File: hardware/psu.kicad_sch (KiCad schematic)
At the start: 35 parts, among them J1 12V Barrel, J2 12V Screw Terminal, Q1 FDS4435BZ, U1 NCP1117-3.3_SOT223, U2 AP64501SP-13

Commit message: Switch AP64501 to standard KiCad SOIC-8-EP footprint
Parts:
- U2: footprint granit:SOIC-8-1EP_3.9x4.9mm_P1.27mm_EP2.95x4.9mm_Mask2.71x3.4mm_ThermalVias -> Package_SO:SOIC-8-1EP_3.9x4.9mm_P1.27mm_EP2.95x4.9mm_Mask2.71x3.4mm_ThermalVias
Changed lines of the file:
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@@
 			)
 		)
-		(property "Footprint" "granit:SOIC-8-1EP_3.9x4.9mm_P1.27mm_EP2.95x4.9mm_Mask2.71x3.4mm_ThermalVias"
+		(property "Footprint" "Package_SO:SOIC-8-1EP_3.9x4.9mm_P1.27mm_EP2.95x4.9mm_Mask2.71x3.4mm_ThermalVias"
 			(at 142.24 127 0)
 			(hide yes)

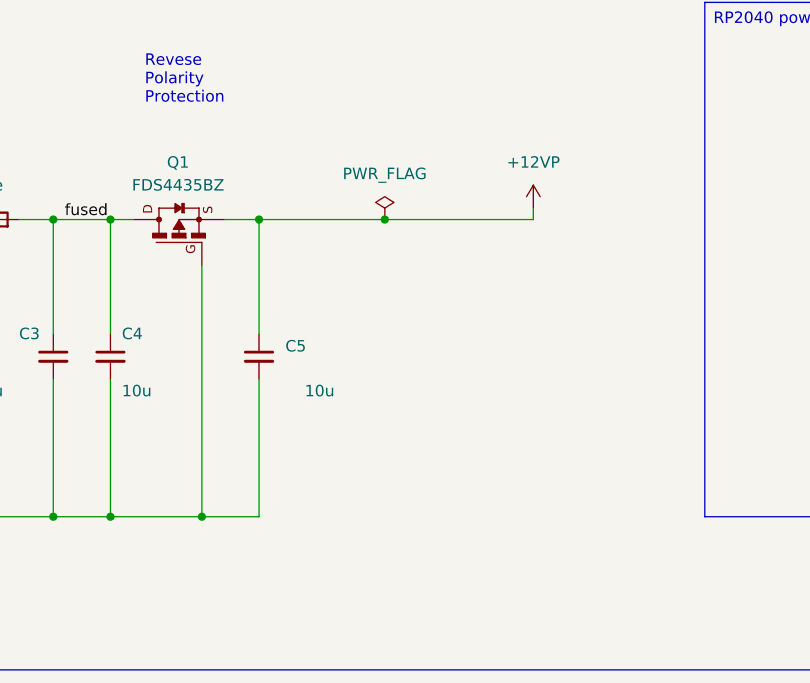
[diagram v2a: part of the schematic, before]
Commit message: Fix mechanical assembly: Part.read() for correct placement, fix PCB/HDD rotations and Z layout
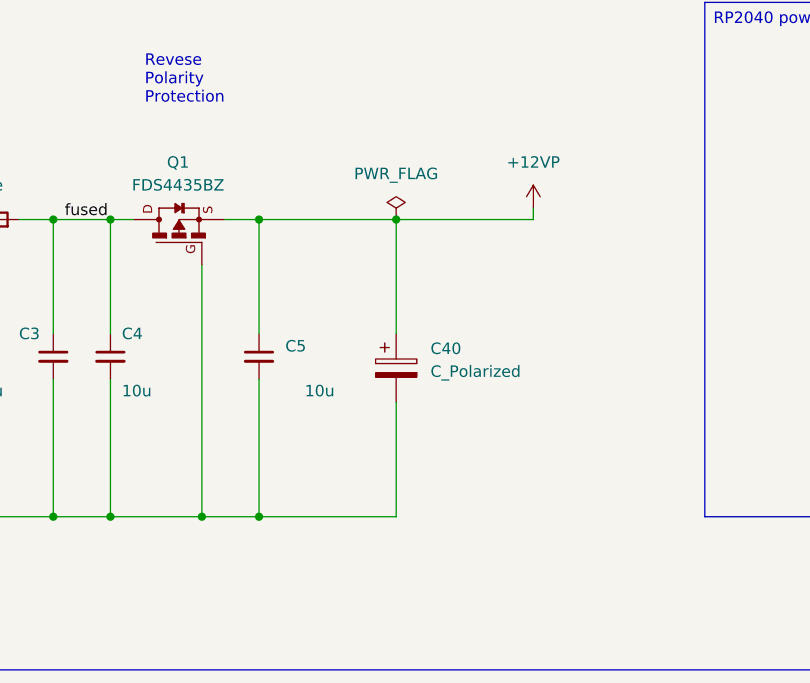
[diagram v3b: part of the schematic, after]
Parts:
- added C40: C_Polarized, symbol Device:C_Polarized
- U2: footprint Package_SO:SOIC-8-1EP_3.9x4.9mm_P1.27mm_EP2.95x4.9mm_Mask2.71x3.4mm_ThermalVias -> granit:SOIC-8-1EP_3.9x4.9mm_P1.27mm_EP2.95x4.9mm_Mask2.71x3.4mm_ThermalVias
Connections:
- net +12VP: now also C40.1
- net GND: now also C40.2
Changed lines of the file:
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@@
 	)
 	(junction
-		(at 102.87 44.45)
+		(at 118.11 44.45)
 		(diameter 0)
 		(color 0 0 0 0)
 	)
 	(junction
-		(at 86.36 127)
+		(at 102.87 77.47)
+		(diameter 0)
+		(color 0 0 0 0)
+	)
+	(junction
+		(at 102.87 44.45)
 		(diameter 0)
 		(color 0 0 0 0)
 	)
 	(junction
-		(at 116.84 44.45)
+		(at 86.36 127)
 		(diameter 0)
 		(color 0 0 0 0)
@@
 	(wire
 		(pts
-			(xy 116.84 44.45) (xy 133.35 44.45)
-		)
-		(stroke
-			(width 0)
-			(type default)
-		)
-	)
-	(wire
-		(pts
 			(xy 179.07 113.03) (xy 179.07 119.38)
 		)
@@
 	(wire
 		(pts
+			(xy 102.87 77.47) (xy 118.11 77.47)
+		)
+		(stroke
+			(width 0)
+			(type default)
+		)
+	)
+	(wire
+		(pts
 			(xy 107.95 127) (xy 119.38 127)
 		)
@@
 	(wire
 		(pts
-			(xy 102.87 44.45) (xy 116.84 44.45)
+			(xy 102.87 44.45) (xy 118.11 44.45)
 		)
 		(stroke
@@
 	(wire
 		(pts
+			(xy 118.11 44.45) (xy 118.11 57.15)
+		)
+		(stroke
+			(width 0)
+			(type default)
+		)
+	)
+	(wire
+		(pts
 			(xy 80.01 62.23) (xy 80.01 77.47)
 		)
@@
 	(wire
 		(pts
+			(xy 118.11 64.77) (xy 118.11 77.47)
+		)
+		(stroke
+			(width 0)
+			(type default)
+		)
+	)
+	(wire
+		(pts
 			(xy 222.25 48.26) (xy 212.09 48.26)
 		)
@@
 		)
 	)
+	(wire
+		(pts
+			(xy 118.11 44.45) (xy 133.35 44.45)
+		)
+		(stroke
+			(width 0)
+			(type default)
+		)
+	)
 	(polyline
 		(pts
@@
 	(symbol
 		(lib_id "power:PWR_FLAG")
-		(at 116.84 44.45 0)
+		(at 118.11 44.45 0)
 		(unit 1)
 		(body_style 1)
@@
 		(fields_autoplaced yes)
 		(property "Reference" "#FLG01"
-			(at 116.84 42.545 0)
+			(at 118.11 42.545 0)
 			(hide yes)
 			(show_name no)
@@
 		)
 		(property "Value" "PWR_FLAG"
-			(at 116.84 39.37 0)
+			(at 118.11 39.37 0)
 			(show_name no)
 			(do_not_autoplace no)
@@
 		)
 		(property "Footprint" ""
-			(at 116.84 44.45 0)
+			(at 118.11 44.45 0)
 			(hide yes)
 			(show_name no)
@@
 		)
 		(property "Datasheet" ""
-			(at 116.84 44.45 0)
+			(at 118.11 44.45 0)
 			(hide yes)
 			(show_name no)
@@
 		)
 		(property "Description" "Special symbol for telling ERC where power comes from"
-			(at 116.84 44.45 0)
+			(at 118.11 44.45 0)
 			(hide yes)
 			(show_name no)
@@
 			)
 		)
-		(property "Footprint" "Package_SO:SOIC-8-1EP_3.9x4.9mm_P1.27mm_EP2.95x4.9mm_Mask2.71x3.4mm_ThermalVias"
+		(property "Footprint" "granit:SOIC-8-1EP_3.9x4.9mm_P1.27mm_EP2.95x4.9mm_Mask2.71x3.4mm_ThermalVias"
 			(at 142.24 127 0)
 			(hide yes)
@@
 					(unit 1)
 				)
+			)
+		)
+	)
+	(symbol
+		(lib_id "Device:C_Polarized")
+		(at 118.11 60.96 0)
+		(unit 1)
+		(body_style 1)
+		(exclude_from_sim no)
+		(in_bom yes)
+		(on_board yes)
+		(in_pos_files yes)
+		(dnp no)
+		(fields_autoplaced yes)
+		(property "Reference" "C40"
+			(at 121.92 58.8009 0)
+			(show_name no)
+			(do_not_autoplace no)
+			(effects
+				(font
+					(size 1.27 1.27)
+				)
+				(justify left)
+			)
+		)
+		(property "Value" "C_Polarized"
+			(at 121.92 61.3409 0)
+			(show_name no)
+			(do_not_autoplace no)
+			(effects
+				(font
+					(size 1.27 1.27)
+				)
+				(justify left)
+			)
+		)
+		(property "Footprint" ""
+			(at 119.0752 64.77 0)
+			(hide yes)
+			(show_name no)
+			(do_not_autoplace no)
+			(effects
+				(font
+					(size 1.27 1.27)
+				)
+			)
+		)
+		(property "Datasheet" ""
+			(at 118.11 60.96 0)
+			(hide yes)
+			(show_name no)
+			(do_not_autoplace no)
+			(effects
+				(font
+					(size 1.27 1.27)
+				)
+			)
+		)
+		(property "Description" "Polarized capacitor"
+			(at 118.11 60.96 0)
+			(hide yes)
+			(show_name no)
+			(do_not_autoplace no)
+			(effects
+				(font
+					(size 1.27 1.27)
+				)
+			)
+		)
+		(pin "2"
+		)
+		(pin "1"
+		)
+		(instances
+			(project "granit"
+				(path "/d2c135e3-a983-4cd4-8cff-b50ca3c7671a/5c34f141-50d5-4609-a101-f9d94643eff8"
+					(reference "C40")
+					(unit 1)
+				)

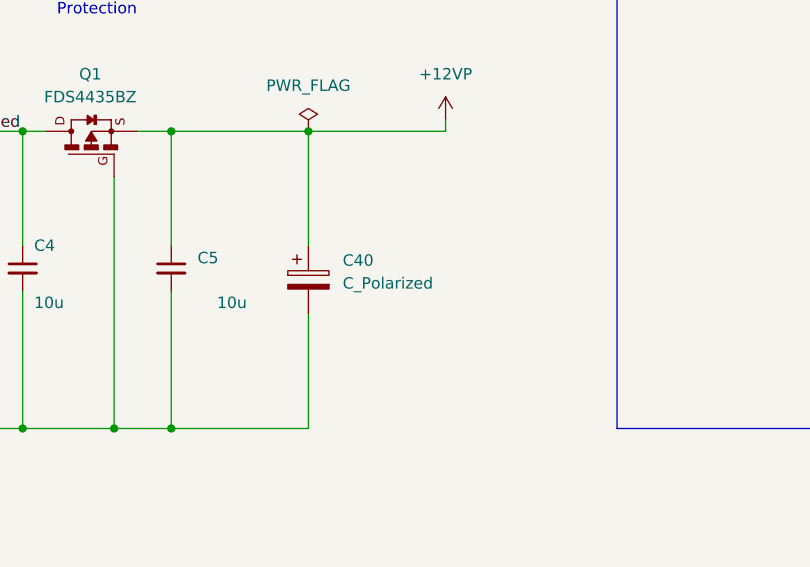
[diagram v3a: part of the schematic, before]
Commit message: Add 100µF/25V bulk capacitor (C40) on 12V rail
Absorbs HDD spin-up inrush current without drooping the buck converter
input. Placed on the fused net after Q1, before the branch to U2 and
SATA power FETs.
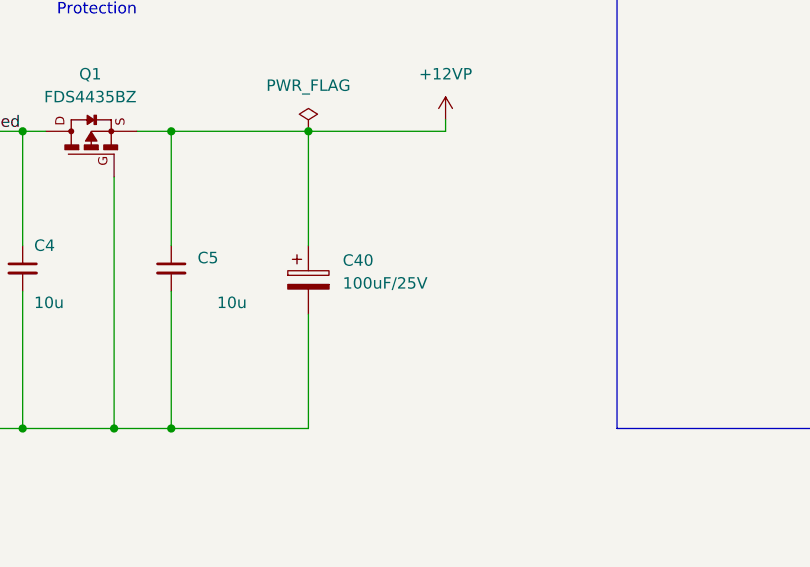
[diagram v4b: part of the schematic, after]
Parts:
- C40: value C_Polarized -> 100uF/25V; footprint (none) -> Capacitor_SMD:CP_Elec_6.3x5.8
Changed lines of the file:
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@@
 			)
 		)
-		(property "Value" "C_Polarized"
+		(property "Value" "100uF/25V"
 			(at 121.92 61.3409 0)
 			(show_name no)
@@
 			)
 		)
-		(property "Footprint" ""
+		(property "Footprint" "Capacitor_SMD:CP_Elec_6.3x5.8"
 			(at 119.0752 64.77 0)
 			(hide yes)

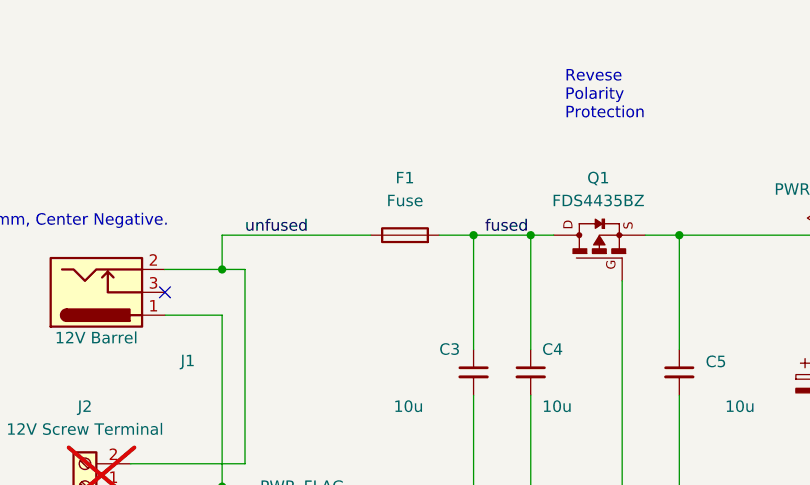
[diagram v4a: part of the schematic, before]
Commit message: fix: add missing BOM values for F1 (3A), Y1 (25MHz), BT1 (CR2032)
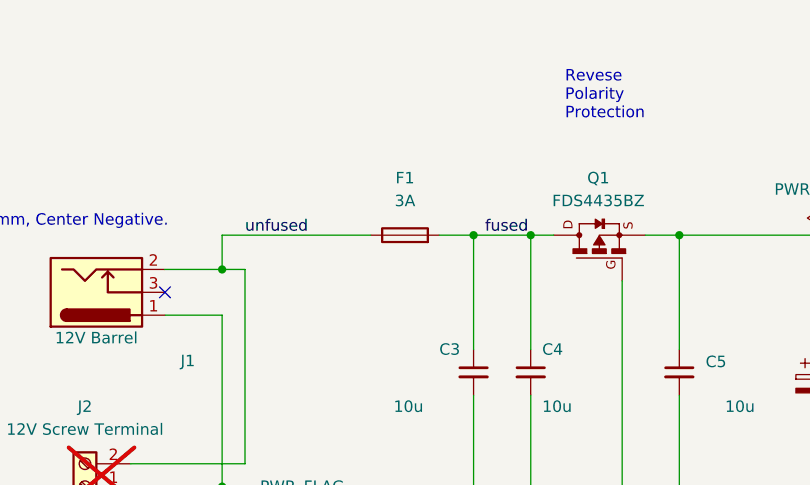
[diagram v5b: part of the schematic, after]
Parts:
- F1: value Fuse -> 3A
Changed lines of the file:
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@@
 			)
 		)
-		(property "Value" "Fuse"
+		(property "Value" "3A"
 			(at 72.39 40.64 90)
 			(show_name no)
